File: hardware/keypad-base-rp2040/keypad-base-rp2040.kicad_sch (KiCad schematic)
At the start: 59 parts, among them J1 USB_C_Receptacle_USB2.0, J2 Conn_01x02, J3 Conn_01x02, Q1 AO3400A, SW1 Switch_SW_Push, SW2 Switch_SW_Push, SW3 Switch_SW_Push, SW4 Switch_SW_Push, SW5 Switch_SW_Push, SW6 Switch_SW_Push, SW7 Switch_SW_Push, SW8 Switch_SW_Push, U1 RP2040, U10 AP2112K-3.3, U11 W25Q128JVS, U3 IE096HQ1301CL, U4 IE096HQ1301CL, U5 IE096HQ1301CL, U6 IE096HQ1301CL, U7 IE096HQ1301CL, U8 IE096HQ1301CL, X1 16MHz

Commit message: hardware/keypad-base-rp2040: progress commit
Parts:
- removed C1, C11, C12, C13, C14, C15, C17, C20, C3, C4, C8: 0.1uF/6.3V, tom-passives:C_0805_2012Metric, symbol tom-passives:C
- removed C16, C18: 1uF/6.3V, tom-passives:C_0805_2012Metric, symbol tom-passives:C
- removed C2, C5: 18pF, tom-passives:C_0805_2012Metric, symbol tom-passives:C
- removed C9: 10uF/10V, tom-passives:C_0805_2012Metric, symbol tom-passives:C
- removed J2, J3: Conn_01x02, tom-connectors:PinHeader_1x02_P2.54mm_Vertical, symbol tom-connectors:Conn_01x02
- removed R1, R11, R12, R2, R3, R4: 10k, tom-passives:R_0805_2012Metric, symbol tom-passives:R
- removed R10, R5, R6, R7, R8, R9: 470R, tom-passives:R_0805_2012Metric, symbol tom-passives:R
- removed R13, R14: 5.1k, tom-passives:R_0805_2012Metric, symbol tom-passives:R
- removed R15, R16: 22R, tom-passives:R_0805_2012Metric, symbol tom-passives:R
- removed X1: 16MHz, tom-passives:Crystal_SMD_5032-2Pin_5.0x3.2mm, symbol tom-passives:CRYSTAL
- added C1, C2: 20pF,50V,C0G, tom-passives:C_0402_1005Metric, symbol jlcpcb-basic-capacitor-0402:20pF,50V,C0G
- added C10, C11, C12, C13, C14, C3, C4, C6, C7, C8: 100nF,16V,X7R, tom-passives:C_0402_1005Metric, symbol jlcpcb-basic-capacitor-0402:100nF,16V,X7R
- added C15, C17, C19, C20, C21, C22, C5: 10uF,6.3V,X5R, tom-passives:C_0402_1005Metric, symbol jlcpcb-basic-capacitor-0402:10uF,6.3V,X5R
- added C16, C18: 1uF,25V,X5R, tom-passives:C_0402_1005Metric, symbol jlcpcb-basic-capacitor-0402:1uF,25V,X5R
- added C9: 10uF,10V,X5R, tom-passives:C_0603_1608Metric, symbol jlcpcb-basic-capacitor-0603:10uF,10V,X5R
- added J3: Conn_02x05_SWD, tom-connectors:FTSH-105-01-F-DV-K, symbol tom-connectors:Conn_02x05_SWD
- added R1, R14: 1k, tom-passives:R_0402_1005Metric, symbol jlcpcb-basic-resistor-0402:1k
- added R10, R11, R12, R13, R6, R9: 470, tom-passives:R_0402_1005Metric, symbol jlcpcb-basic-resistor-0402:470
- added R15, R7, R8: 10k, tom-passives:R_0402_1005Metric, symbol jlcpcb-basic-resistor-0402:10k
- added R2, R5: 5.1k, tom-passives:R_0402_1005Metric, symbol jlcpcb-basic-resistor-0402:5.1k
- added R3, R4: 27, tom-passives:R_0603_1608Metric, symbol jlcpcb-basic-resistor-0603:27
- added SW9: Switch_SW_Push, tom-mechanical:SW_SPST_SMD_SIDE_C319395, symbol tom-mechanical:SW_SPST
- added X1: 12MHz, tom-passives:Crystal_SMD_3225-4Pin_3.2x2.5mm, symbol tom-passives:CRYSTAL_4PIN
- J1: LCSC (none) -> C709357
- SW1: renamed from SW2; LCSC (none) -> C2803348
- SW2: renamed from SW3; LCSC (none) -> C2803348
- SW3: renamed from SW4; LCSC (none) -> C2803348
- SW4: renamed from SW5; LCSC (none) -> C2803348
- SW5: renamed from SW6; LCSC (none) -> C2803348
- SW6: renamed from SW7; LCSC (none) -> C2803348
- SW7: renamed from SW8; footprint tom-mechanical:SW_SPST_SMD_SIDE_7.0x3.5 -> tom-mechanical:SW_SPST_SMD_SIDE_C319395; LCSC (none) -> C319395
- SW8: renamed from SW1; footprint tom-mechanical:SW_SPST_SMD_SIDE_7.0x3.5 -> tom-mechanical:SW_SPST_SMD_SIDE_C319395; LCSC (none) -> C319395
- U1: LCSC (none) -> C2040
- U10: LCSC (none) -> C51118
- U11: LCSC (none) -> C97521
- renumbered U6 to U5, U5 to U6
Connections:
- net MISO is gone; now on net QSPI_SD1: U11.2 (DO(IO1))
- net SCK is gone; now on net QSPI_SCLK: U11.6 (CLK)
- net SCL is gone; now on net SCLK: U3.4 (SCL), U4.4 (SCL), U5.4 (SCL), U6.4 (SCL), U7.4 (SCL), U8.4 (SCL)
- net SDA is gone; now on net MOSI: U3.3 (SDA), U4.3 (SDA), U5.3 (SDA), U6.3 (SDA), U7.3 (SDA), U8.3 (SDA)
- net ~{FLASH_CS} is gone; now on net QSPI_SS: U11.1 (~{CS})
- net +3.3V: now also U1.1 (IOVDD), U1.10 (IOVDD), U1.22 (IOVDD), U1.33 (IOVDD), U1.42 (IOVDD), U1.44 (VREG_IN), U1.48 (USB_VDD), U1.49 (IOVDD), C10.1, C11.1, C12.1, C13.1, C14.1, C15.1, C17.1, C18.1, C19.1, C20.1, C21.1, C22.1, C6.1, C7.1, C8.1, J3.1 (VCC), R7.1, R8.1
- net +5V: now also C16.1, C9.1
- net BACKLIGHT: now also U1.32 (GPIO21), R15.1
- net BACKLIGHTK: now also R10.2, R11.2, R12.2, R13.2, R6.2, R9.2
- net CC1: now also R2.1
- net CC2: now also R5.1
- net D\C: now also U1.34 (GPIO22)
- net D_N: now also R3.2
- net D_P: now also R4.2
- net GND: now also U1.19 (TESTEN), U1.57 (GND), C1.2, C10.2, C11.2, C12.2, C13.2, C14.2, C15.2, C16.2, C17.2, C18.2, C19.2, C2.2, C20.2, C21.2, C22.2, C3.2, C4.2, C5.2, C6.2, C7.2, C8.2, C9.2, J3.3 (GND), J3.5 (GND), J3.9 (GND), R15.2, R2.2, R5.2, SW9.1 (A), X1.2 (GND), X1.4 (GND)
- net MOSI: now also U1.5 (GPIO3); no longer U11.5 (DI(IO0))
- net SW1: now also SW1.2, U1.11 (GPIO8); no longer SW8.2 (B)
- net SW2: now also SW2.2, U1.12 (GPIO9); no longer SW1.2
- net SW3: now also SW3.2, U1.13 (GPIO10); no longer SW2.2
- net SW4: now also SW4.2, U1.14 (GPIO11); no longer SW3.2
- net SW5: now also SW5.2, U1.15 (GPIO12); no longer SW4.2
- net SW6: now also SW6.2, U1.16 (GPIO13); no longer SW5.2
- net SW7: now also SW7.2 (B), U1.17 (GPIO14); no longer SW6.2
- net SW8: now also SW8.2 (B), U1.18 (GPIO15); no longer SW7.2 (B)
- net USB_N: now also U1.46 (USB_DM), R3.1
- net USB_P: now also U1.47 (USB_DP), R4.1
- net ~{CS1}: now also U1.41 (GPIO29_ADC3)
- net ~{CS2}: now also U1.40 (GPIO28_ADC2)
- net ~{CS3}: now also U1.39 (GPIO27_ADC1)
- net ~{CS4}: now also U1.38 (GPIO26_ADC0)
- net ~{CS5}: now also U1.36 (GPIO24)
- net ~{CS6}: now also U1.35 (GPIO23)
- net ~{LCDRESET}: now also U1.31 (GPIO20)
- net ~{RESET}: now also U1.26 (RUN), J3.10 (RESET), R7.2
- net QSPI_SD2: now reaches U11.3 (IO2)
- net QSPI_SD2: now also U1.54 (QSPI_SD2)
- net QSPI_SD3: now reaches U11.7 (IO3)
- net QSPI_SD3: now also U1.51 (QSPI_SD3)
- net at U3.11 (LEDK): now also R6.1
- net at U4.11 (LEDK): now also R9.1
- net at U5.11 (LEDK): now also R10.1
- net at U6.11 (LEDK): now also R11.1
- net at U7.11 (LEDK): now also R12.1
- net at U8.11 (LEDK): now also R13.1
- net XIN: now reaches U1.20 (XIN)
- net XIN: now also C1.1, X1.1
- net XOUT: now reaches U1.21 (XOUT)
- net XOUT: now also R1.1
- net +1V1: now reaches U1.23 (DVDD)
- net +1V1: now also U1.45 (VREG_VOUT), U1.50 (DVDD), C3.1, C4.1, C5.1
- net SWCLK: now reaches U1.24 (SWCLK)
- net SWCLK: now also J3.4 (SWDCLK)
- net SWD: now reaches U1.25 (SWD)
- net SWD: now also J3.2 (SWDIO)
- net SCLK: now reaches U1.4 (GPIO2)
- net QSPI_SCLK: now reaches U1.52 (QSPI_SCLK)
- net QSPI_SD0: now reaches U1.53 (QSPI_SD0)
- net QSPI_SD0: now also U11.5 (DI(IO0))
- net QSPI_SD1: now reaches U1.55 (QSPI_SD1)
- net QSPI_SS: now reaches U1.56 (QSPI_SS)
- net QSPI_SS: now also R14.1, R8.2
- new net: C2.1, R1.2, X1.3
- new net BOOTSEL: R14.2, SW9.2 (B)
- no-connect marks 14 -> 16
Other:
- moved on the sheet: J1, SW1, SW2, SW3, SW4, SW5, SW6, SW7, SW8, U11

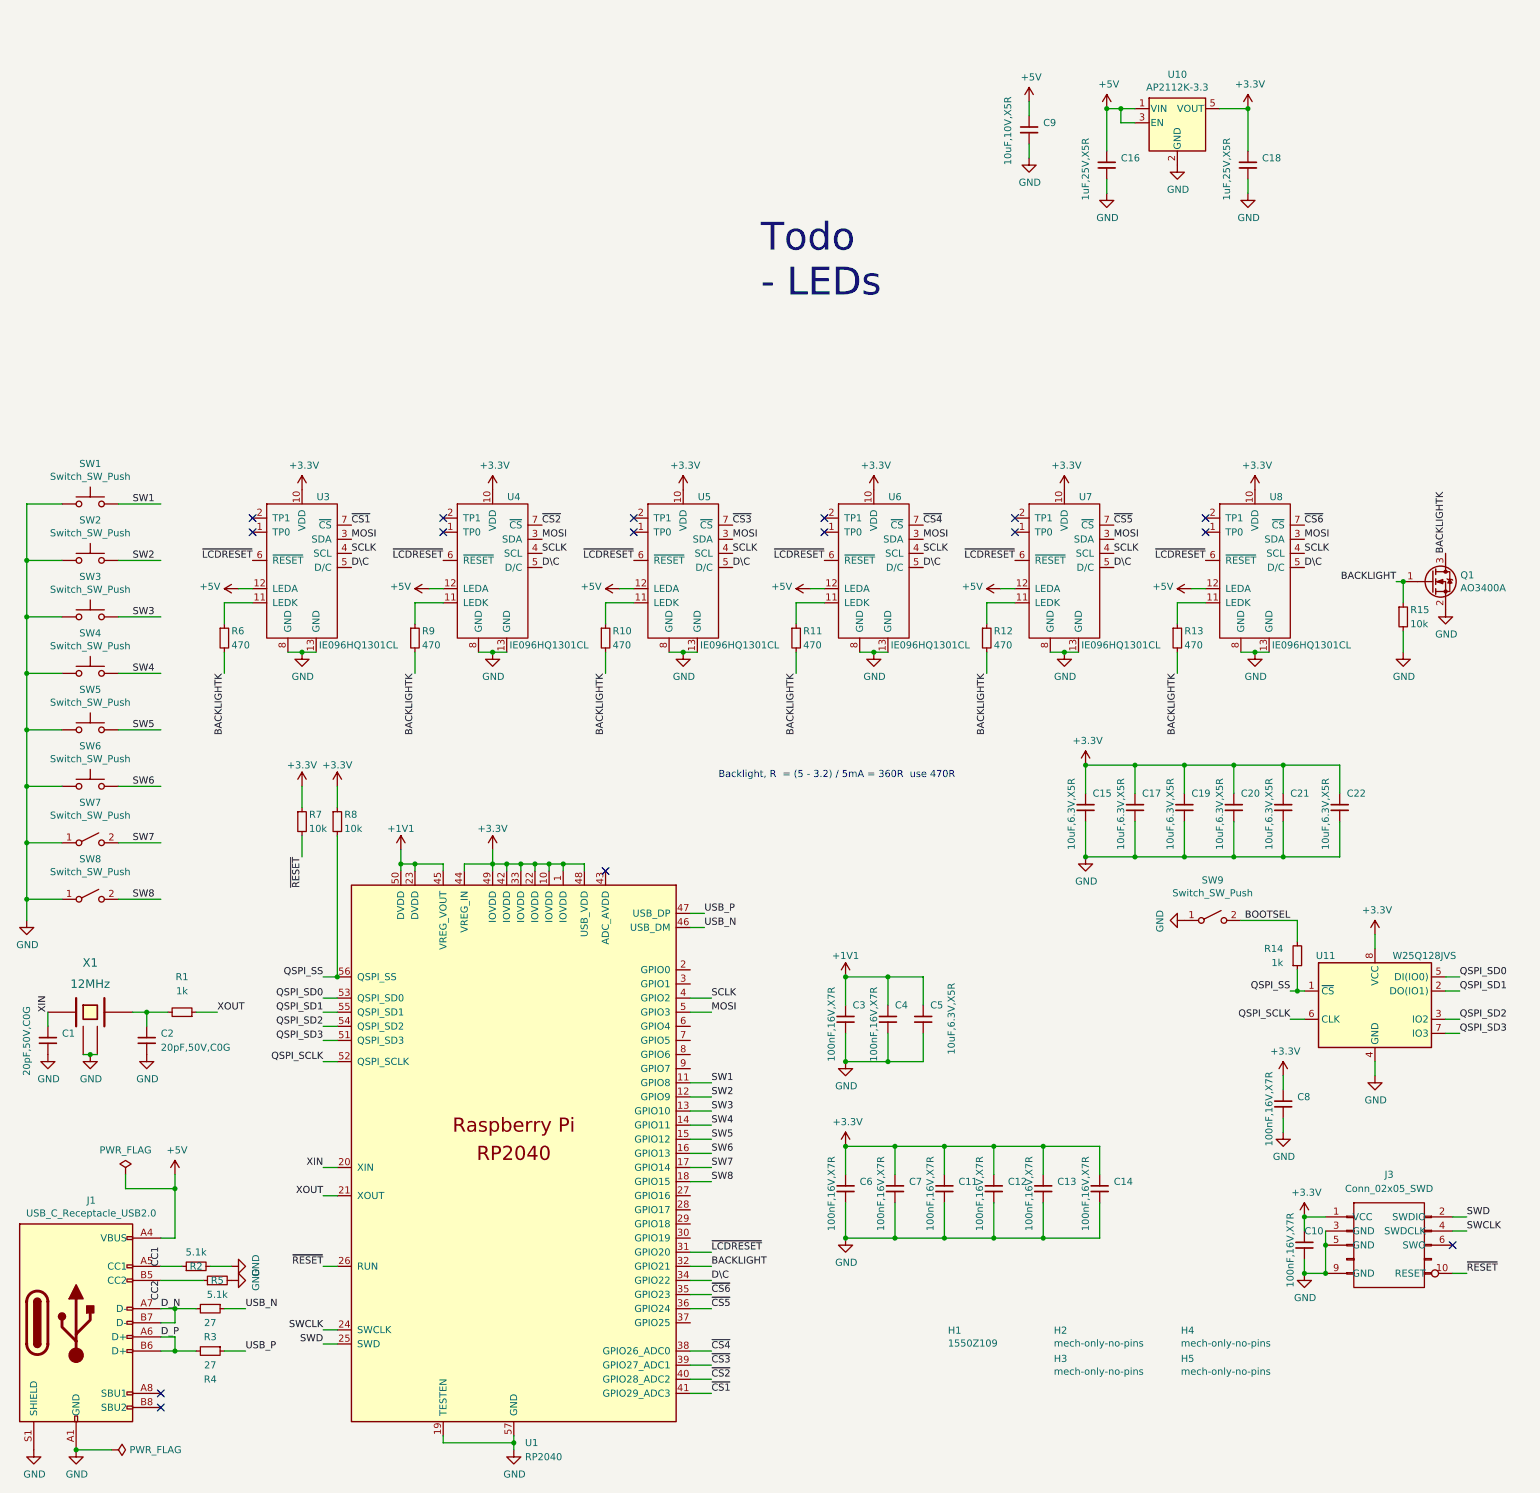
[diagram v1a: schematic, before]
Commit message: hardware/keypad-base-rp2040: placed, routed, ERC & DRC clean
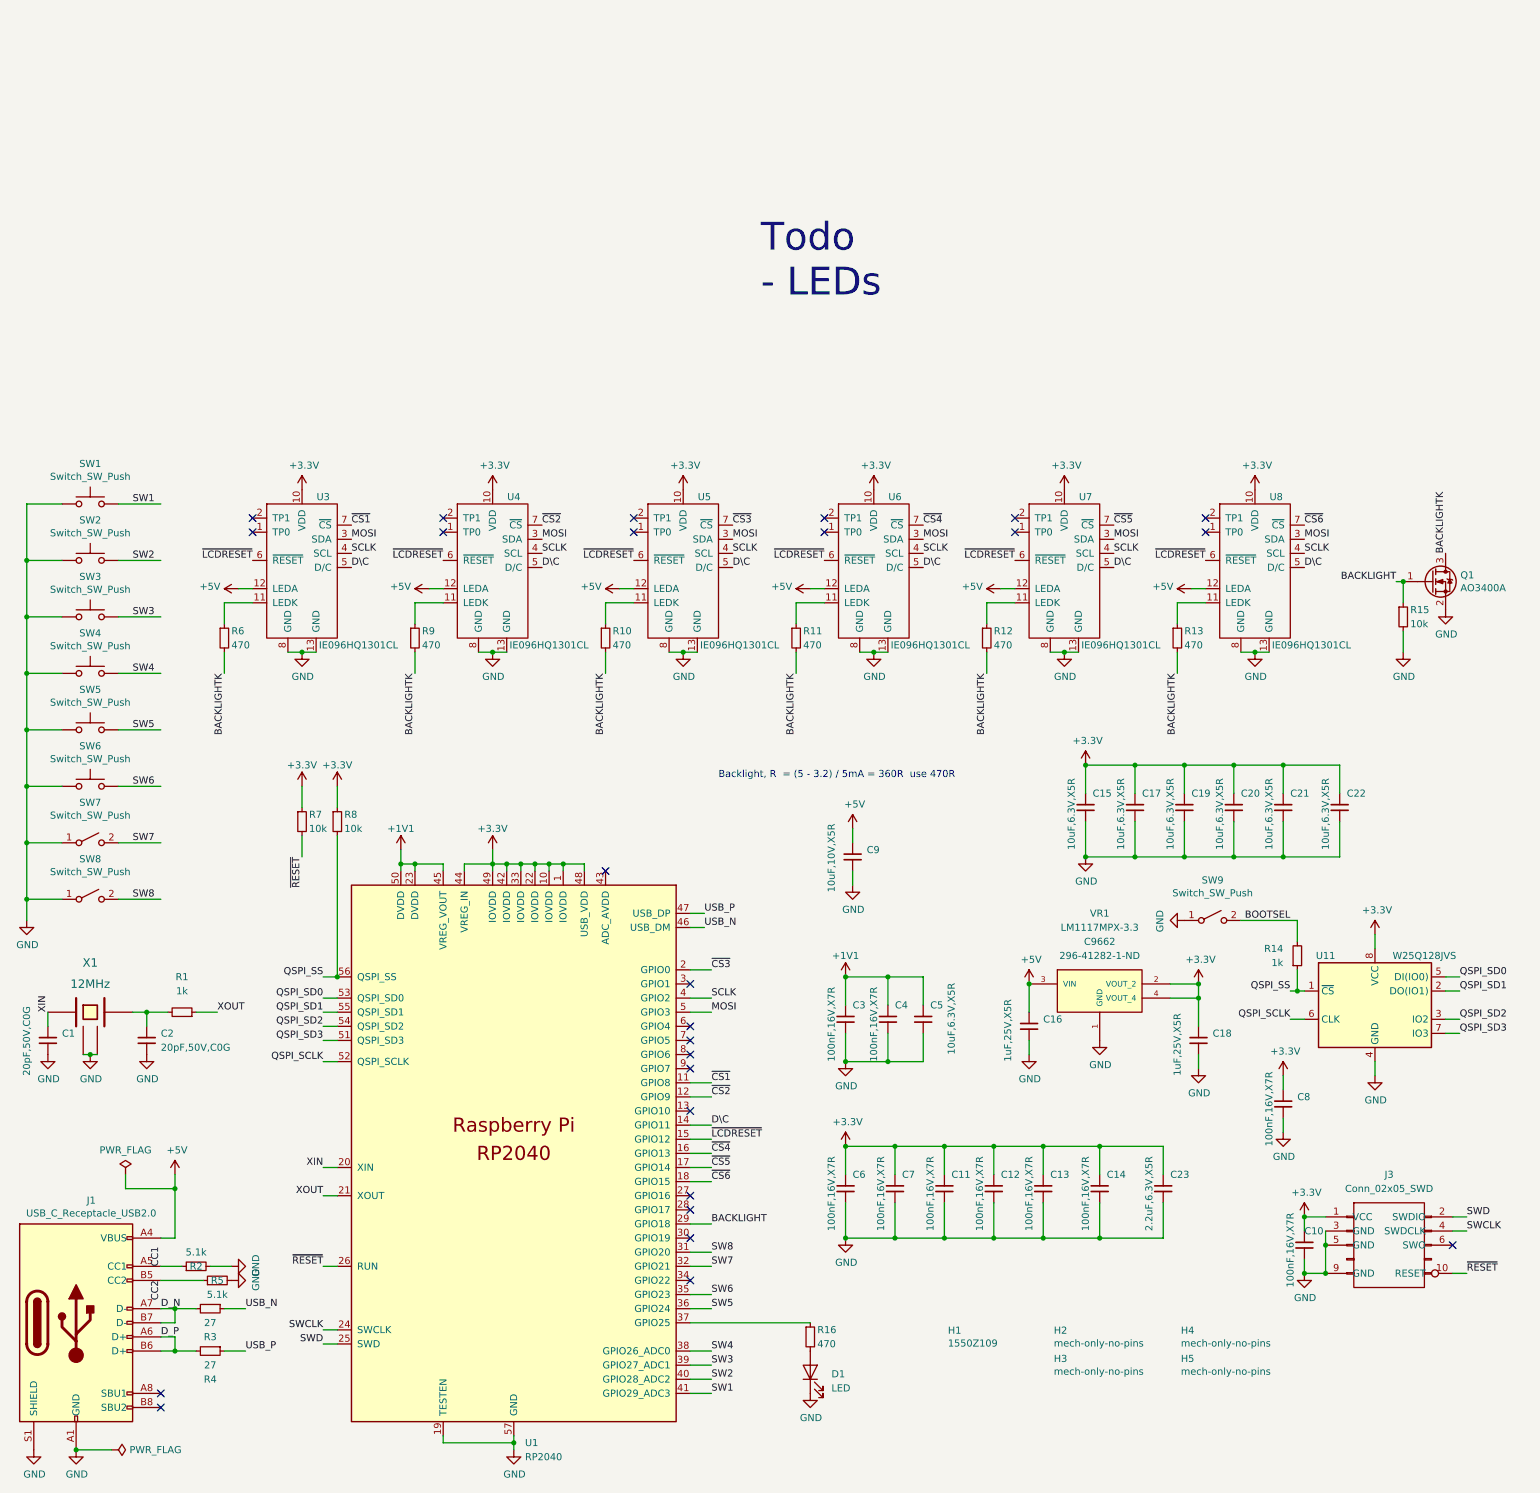
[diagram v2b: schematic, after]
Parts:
- removed U10: AP2112K-3.3, tom-semiconductors:SOT-23-5, symbol tom-semiconductors:AP2112K-3.3
- added C23: 2.2uF,6.3V,X5R, tom-passives:C_0402_1005Metric, symbol jlcpcb-basic-capacitor-0402:2.2uF,6.3V,X5R
- added D1: LED, tom-opto:LED_0805_2012Metric, symbol tom-opto:LED
- added R16: 470, tom-passives:R_0402_1005Metric, symbol jlcpcb-basic-resistor-0402:470
- added VR1: LM1117MPX-3.3, tom-semiconductors:VREG_LM1117MPX-3.3, symbol tom-semiconductors:LM1117MPX-3.3
- Q1: LCSC (none) -> C20917
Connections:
- net +3.3V: now also C23.1, VR1.2 (VOUT_2), VR1.4 (VOUT_4)
- net +5V: now also VR1.3 (VIN)
- net BACKLIGHT: now also U1.29 (GPIO18); no longer U1.32 (GPIO21)
- net D\C: now also U1.14 (GPIO11); no longer U1.34 (GPIO22)
- net GND: now also C23.2, D1.1 (K), VR1.1 (GND)
- net SW1: now also U1.41 (GPIO29_ADC3); no longer U1.11 (GPIO8)
- net SW2: now also U1.40 (GPIO28_ADC2); no longer U1.12 (GPIO9)
- net SW3: now also U1.39 (GPIO27_ADC1); no longer U1.13 (GPIO10)
- net SW4: now also U1.38 (GPIO26_ADC0); no longer U1.14 (GPIO11)
- net SW5: now also U1.36 (GPIO24); no longer U1.15 (GPIO12)
- net SW6: now also U1.35 (GPIO23); no longer U1.16 (GPIO13)
- net SW7: now also U1.32 (GPIO21); no longer U1.17 (GPIO14)
- net SW8: now also U1.31 (GPIO20); no longer U1.18 (GPIO15)
- net ~{CS1}: now also U1.11 (GPIO8); no longer U1.41 (GPIO29_ADC3)
- net ~{CS2}: now also U1.12 (GPIO9); no longer U1.40 (GPIO28_ADC2)
- net ~{CS3}: now also U1.2 (GPIO0); no longer U1.39 (GPIO27_ADC1)
- net ~{CS4}: now also U1.16 (GPIO13); no longer U1.38 (GPIO26_ADC0)
- net ~{CS5}: now also U1.17 (GPIO14); no longer U1.36 (GPIO24)
- net ~{CS6}: now also U1.18 (GPIO15); no longer U1.35 (GPIO23)
- net ~{LCDRESET}: now also U1.15 (GPIO12); no longer U1.31 (GPIO20)
- net at U1.37 (GPIO25): now also R16.1
- new net: D1.2 (A), R16.2
- no-connect marks 16 -> 26
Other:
- moved on the sheet: C16, C18, C9

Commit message: hardare/keypad-base-rp2040: Sep2022 as submitted
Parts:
- added TP1: TestPoint, tom-mechanical:TestPoint_Pad_D1.0mm, symbol tom-mechanical:TestPoint
- C1, C10, C11, C12, C13, C14, C15, C16, C17, C18, C19, C2, C20, C21, C22, C23, C3, C4, C5, C6, C7, C8: footprint tom-passives:C_0402_1005Metric -> C_0402_1005Metric
- C9: footprint tom-passives:C_0603_1608Metric -> C_0603_1608Metric
- R1, R10, R11, R12, R13, R14, R15, R16, R2, R5, R6, R7, R8, R9: footprint tom-passives:R_0402_1005Metric -> R_0402_1005Metric
- R3, R4: footprint tom-passives:R_0603_1608Metric -> R_0603_1608Metric
- VR1: footprint tom-semiconductors:VREG_LM1117MPX-3.3 -> VREG_LM1117MPX-3.3
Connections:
- net at U1.6 (GPIO4): now also TP1.1
- no-connect marks 26 -> 24
